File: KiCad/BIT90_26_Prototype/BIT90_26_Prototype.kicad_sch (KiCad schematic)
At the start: 0 parts

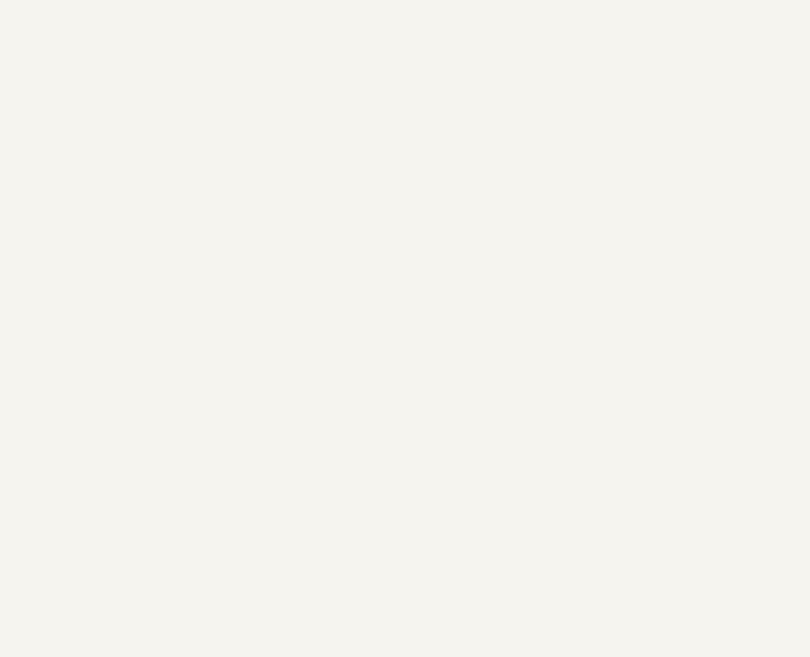
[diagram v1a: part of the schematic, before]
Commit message: Added more signal analysis to schematic
Would be nice to reduce the amount of glue logic
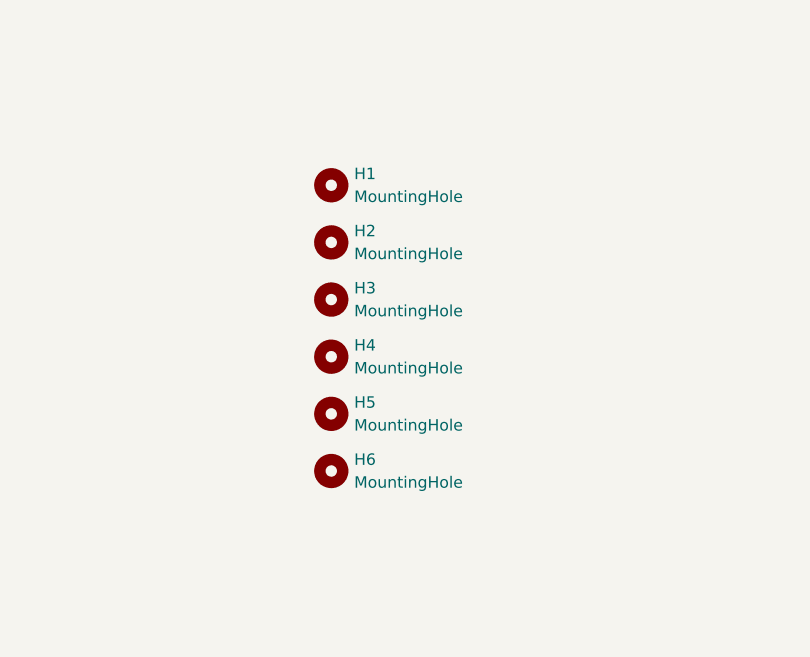
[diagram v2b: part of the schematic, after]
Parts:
- added H1, H2, H3, H4, H5, H6: MountingHole, MountingHole:MountingHole_3.2mm_M3, symbol Mechanical:MountingHole
